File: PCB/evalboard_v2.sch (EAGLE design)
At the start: 63 parts, among them IC1 BQ24074, IC2 LTC3113EFE#PBF, IC3 LTC3130IUDC-1#PBF#2, J1 2604-1102, J2 PJ-031D, J3 2604-1102, Q1 DMP3056L-7#2, Q2 DMG3402L-7, Q3 DMP3056L-7#2, Q4 DMG3402L-7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

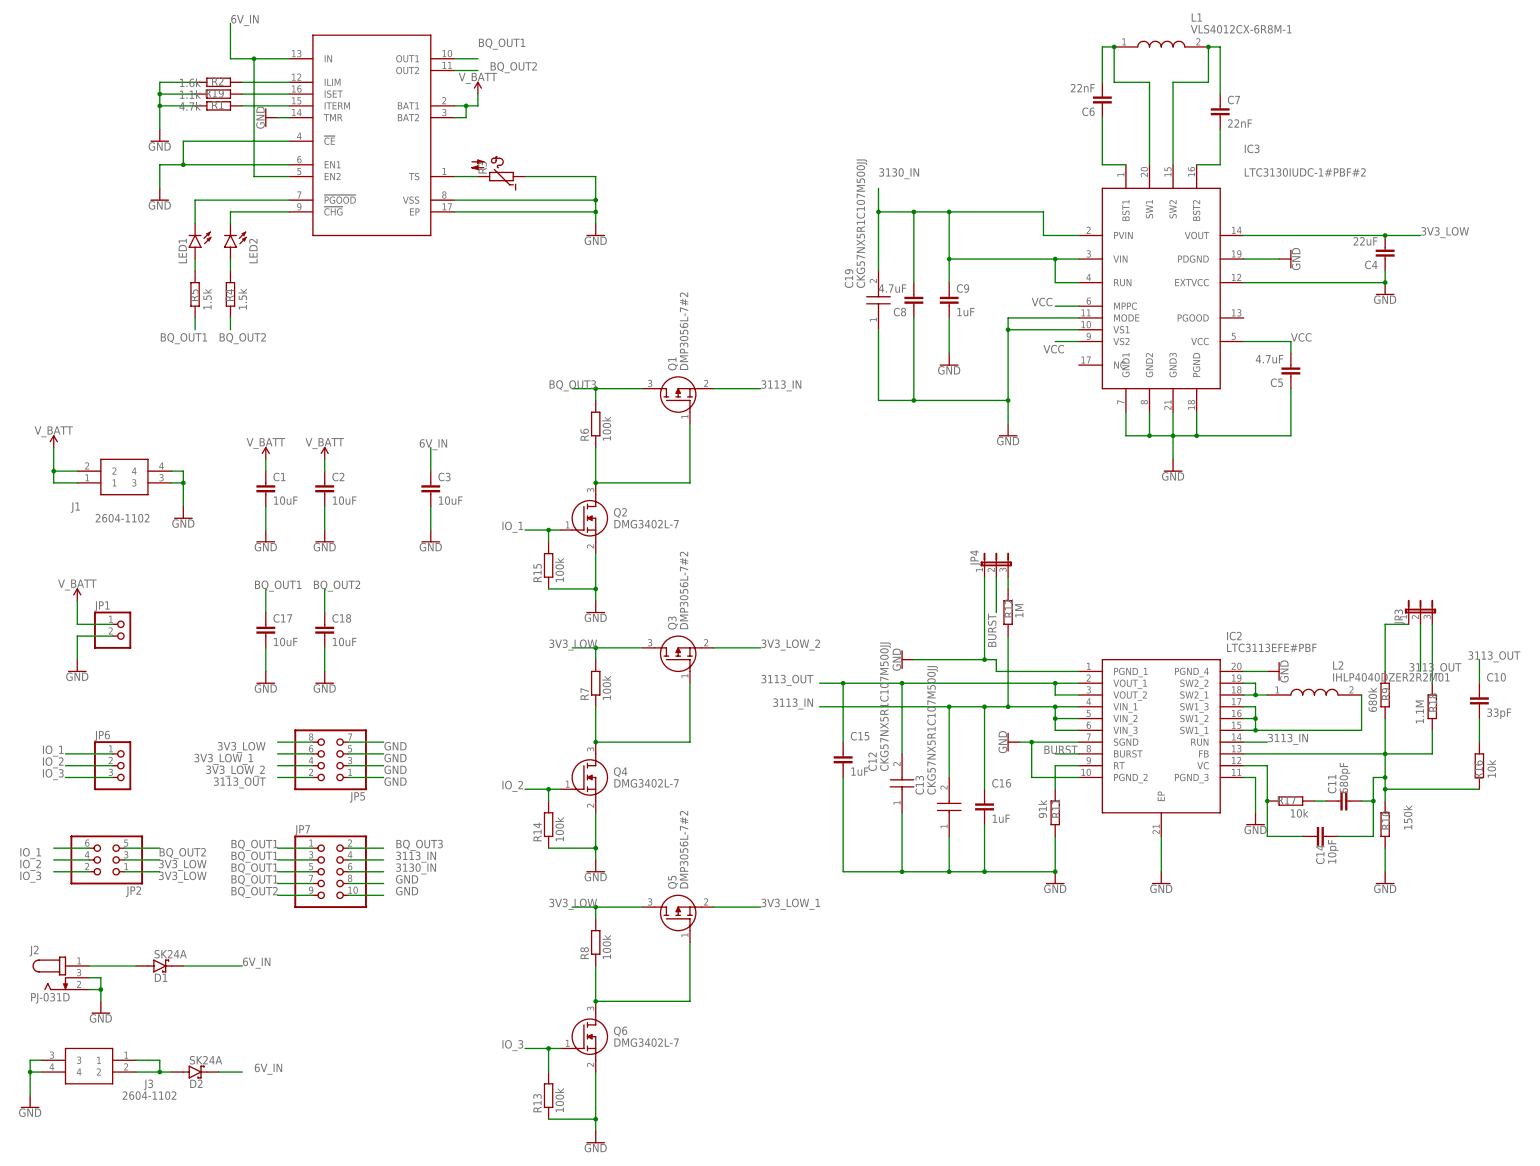
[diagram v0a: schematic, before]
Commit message: Fixed MOSFETs, VS1, VS2, updated README
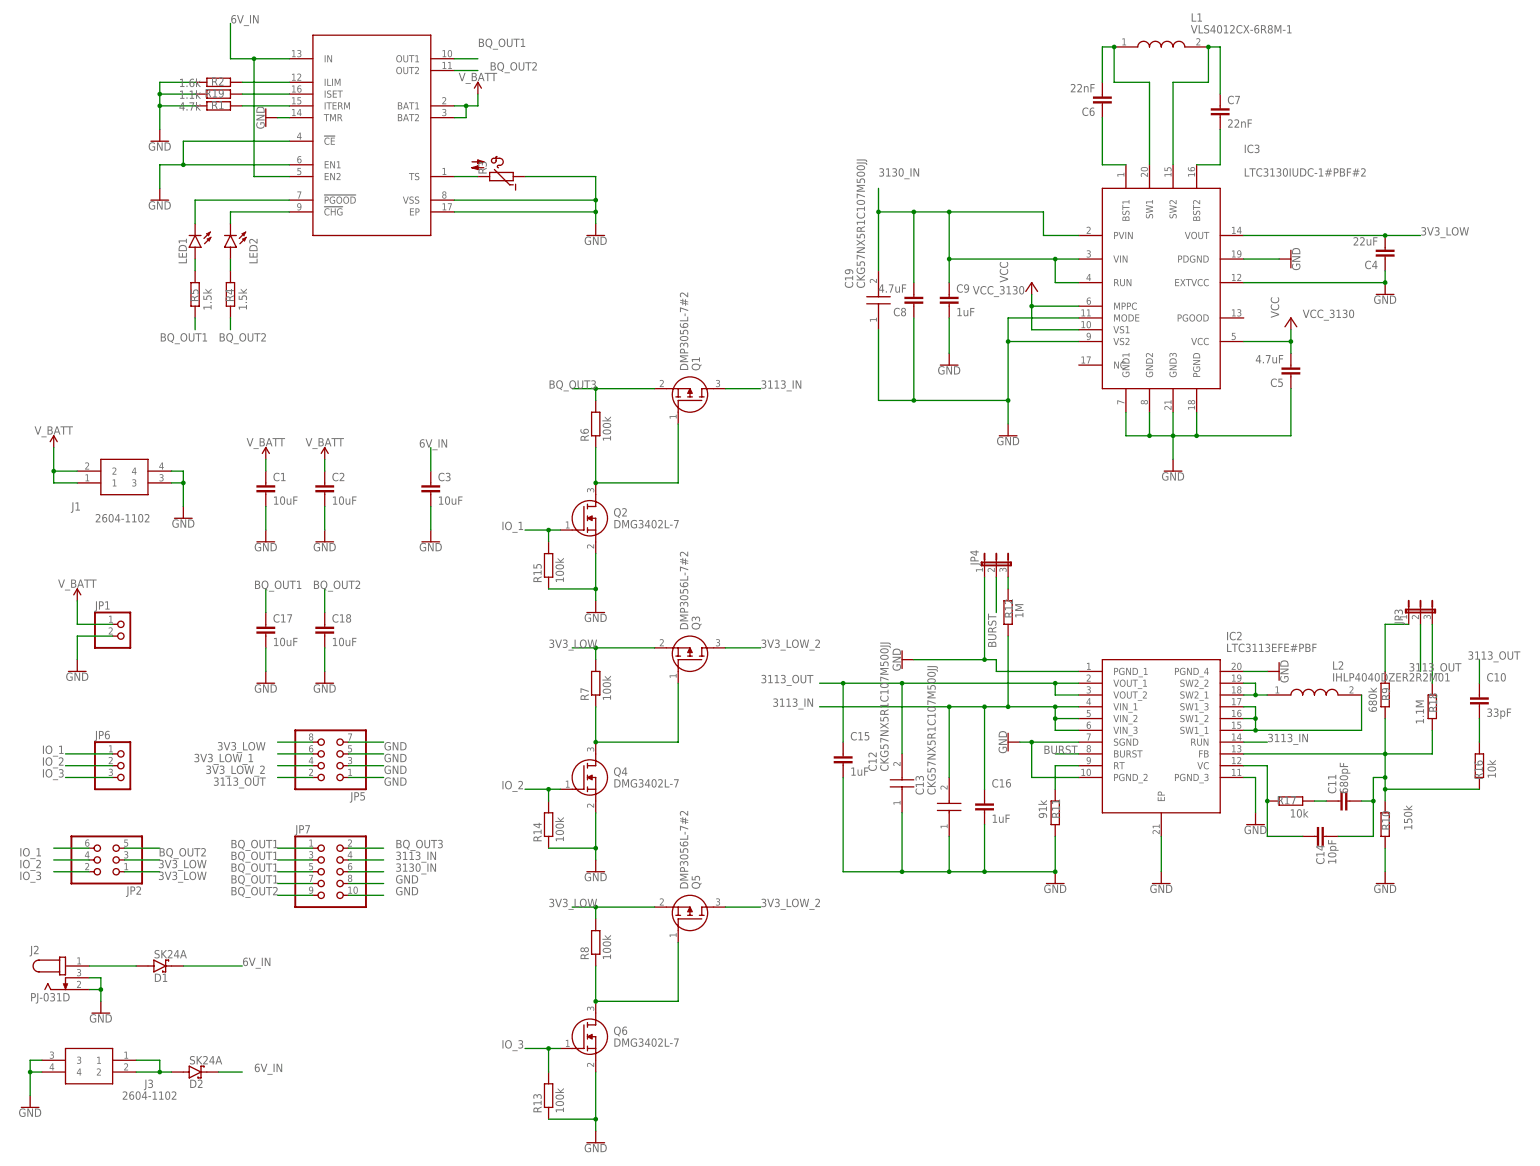
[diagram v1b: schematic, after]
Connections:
- removed net VCC: C5.2, IC3.MPPC, IC3.VCC, IC3.VS2
- new net VCC_3130: C5.2, IC3.MPPC, IC3.VCC, IC3.VS1
- net 3113_IN: now also Q1.D; no longer Q1.S
- net 3V3_LOW: now also Q3.S, Q5.S; no longer Q3.D, Q5.D
- net 3V3_LOW_1: no longer Q5.S
- net 3V3_LOW_2: now also Q3.D, Q5.D; no longer Q3.S
- net BQ_OUT3: now also Q1.S; no longer Q1.D
- net GND: now also IC3.VS2; no longer IC3.VS1
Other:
- moved on the sheet: Q1, Q3, Q5
